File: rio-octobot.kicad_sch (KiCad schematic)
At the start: 48 parts, among them J1 Conn_01x06, J10 Conn_01x03, J2 Conn_01x06, J3 Conn_01x06, J4 Conn_01x06, J5 Conn_01x06, J6 Conn_01x06, J7 Conn_01x06, J8 Conn_01x06, J9 Conn_01x03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

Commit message: fixing labels / add some values
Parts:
- R1: value R -> 10k
- R1: value R -> 1k
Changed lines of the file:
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@@
     (stroke (width 0) (type default))
   )
-  (wire (pts (xy 146.05 60.96) (xy 173.99 60.96))
+  (wire (pts (xy 146.05 59.69) (xy 173.99 59.69))
     (stroke (width 0) (type default))
   )
@@
     (stroke (width 0) (type default))
   )
-  (wire (pts (xy 173.99 60.96) (xy 173.99 58.42))
+  (wire (pts (xy 173.99 59.69) (xy 173.99 58.42))
     (stroke (width 0) (type default))
   )
@@
     (stroke (width 0) (type default))
   )
+  (wire (pts (xy 146.05 53.34) (xy 146.05 59.69))
+    (stroke (width 0) (type default))
+  )
   (wire (pts (xy 210.82 45.72) (xy 210.82 54.61))
     (stroke (width 0) (type default))
@@
     (stroke (width 0) (type default))
   )
-  (wire (pts (xy 146.05 53.34) (xy 146.05 60.96))
-    (stroke (width 0) (type default))
-  )
   (wire (pts (xy 146.05 45.72) (xy 146.05 48.26))
     (stroke (width 0) (type default))
@@
     )
   )
-  (global_label "gnd" (shape input) (at 146.05 53.34 180) (fields_autoplaced)
+  (global_label "gnd" (shape input) (at 146.05 59.69 180) (fields_autoplaced)
     (effects (font (size 1.27 1.27)) (justify right))
-    (property "Intersheetrefs" "${INTERSHEET_REFS}" (at 139.6972 53.34 0)
+    (property "Intersheetrefs" "${INTERSHEET_REFS}" (at 139.6972 59.69 0)
       (effects (font (size 1.27 1.27)) (justify right) hide)
     )
@@
   )
   (symbol (lib_id "Device:R") (at 149.86 45.72 90) (unit 1)
-    (in_bom yes) (on_board yes) (dnp no) (fields_autoplaced)
-    (property "Reference" "R1" (at 149.86 39.37 90)
+    (in_bom yes) (on_board yes) (dnp no)
+    (property "Reference" "R1" (at 143.51 45.72 90)
       (effects (font (size 1.27 1.27)))
     )
-    (property "Value" "R" (at 149.86 41.91 90)
+    (property "Value" "10k" (at 154.94 46.99 90)
       (effects (font (size 1.27 1.27)))
     )
@@
   )
   (symbol (lib_id "Device:R") (at 149.86 38.1 90) (unit 1)
-    (in_bom yes) (on_board yes) (dnp no) (fields_autoplaced)
-    (property "Reference" "R1" (at 149.86 31.75 90)
+    (in_bom yes) (on_board yes) (dnp no)
+    (property "Reference" "R1" (at 143.51 38.1 90)
       (effects (font (size 1.27 1.27)))
     )
-    (property "Value" "R" (at 149.86 34.29 90)
+    (property "Value" "10k" (at 154.94 39.37 90)
       (effects (font (size 1.27 1.27)))
     )
@@
   )
   (symbol (lib_id "Device:R") (at 149.86 50.8 90) (unit 1)
-    (in_bom yes) (on_board yes) (dnp no) (fields_autoplaced)
-    (property "Reference" "R1" (at 149.86 44.45 90)
+    (in_bom yes) (on_board yes) (dnp no)
+    (property "Reference" "R1" (at 143.51 50.8 90)
       (effects (font (size 1.27 1.27)))
     )
-    (property "Value" "R" (at 149.86 46.99 90)
+    (property "Value" "10k" (at 154.94 52.07 90)
       (effects (font (size 1.27 1.27)))
     )
@@
   )
   (symbol (lib_id "Device:R") (at 149.86 53.34 90) (unit 1)
-    (in_bom yes) (on_board yes) (dnp no) (fields_autoplaced)
-    (property "Reference" "R1" (at 149.86 46.99 90)
+    (in_bom yes) (on_board yes) (dnp no)
+    (property "Reference" "R1" (at 143.51 53.34 90)
       (effects (font (size 1.27 1.27)))
     )
-    (property "Value" "R" (at 149.86 49.53 90)
+    (property "Value" "10k" (at 154.94 54.61 90)
       (effects (font (size 1.27 1.27)))
     )
@@
   )
   (symbol (lib_id "Device:R") (at 149.86 43.18 90) (unit 1)
-    (in_bom yes) (on_board yes) (dnp no) (fields_autoplaced)
-    (property "Reference" "R1" (at 149.86 36.83 90)
+    (in_bom yes) (on_board yes) (dnp no)
+    (property "Reference" "R1" (at 143.51 43.18 90)
       (effects (font (size 1.27 1.27)))
     )
-    (property "Value" "R" (at 149.86 39.37 90)
+    (property "Value" "10k" (at 154.94 44.45 90)
       (effects (font (size 1.27 1.27)))
     )
@@
   )
   (symbol (lib_id "Device:R") (at 149.86 40.64 90) (unit 1)
-    (in_bom yes) (on_board yes) (dnp no) (fields_autoplaced)
-    (property "Reference" "R1" (at 149.86 34.29 90)
+    (in_bom yes) (on_board yes) (dnp no)
+    (property "Reference" "R1" (at 143.51 40.64 90)
       (effects (font (size 1.27 1.27)))
     )
-    (property "Value" "R" (at 149.86 36.83 90)
+    (property "Value" "10k" (at 154.94 41.91 90)
       (effects (font (size 1.27 1.27)))
     )
@@
   )
   (symbol (lib_id "Device:R") (at 149.86 48.26 90) (unit 1)
-    (in_bom yes) (on_board yes) (dnp no) (fields_autoplaced)
-    (property "Reference" "R1" (at 149.86 41.91 90)
+    (in_bom yes) (on_board yes) (dnp no)
+    (property "Reference" "R1" (at 143.51 48.26 90)
       (effects (font (size 1.27 1.27)))
     )
-    (property "Value" "R" (at 149.86 44.45 90)
+    (property "Value" "10k" (at 154.94 49.53 90)
       (effects (font (size 1.27 1.27)))
     )
@@
       (effects (font (size 1.27 1.27)))
     )
-    (property "Value" "R" (at 196.85 107.95 90)
+    (property "Value" "1k" (at 196.85 107.95 90)
       (effects (font (size 1.27 1.27)))
     )
@@
       (effects (font (size 1.27 1.27)))
     )
-    (property "Value" "R" (at 201.93 138.43 90)
+    (property "Value" "10k" (at 201.93 138.43 90)
       (effects (font (size 1.27 1.27)))
     )
@@
   )
   (symbol (lib_id "Device:R") (at 187.96 147.32 90) (unit 1)
-    (in_bom yes) (on_board yes) (dnp no) (fields_autoplaced)
-    (property "Reference" "R1" (at 187.96 140.97 90)
+    (in_bom yes) (on_board yes) (dnp no)
+    (property "Reference" "R1" (at 187.96 144.78 90)
       (effects (font (size 1.27 1.27)))
     )
-    (property "Value" "R" (at 187.96 143.51 90)
+    (property "Value" "1k" (at 187.96 149.86 90)
       (effects (font (size 1.27 1.27)))
     )
@@
       (effects (font (size 1.27 1.27)) (justify right))
     )
-    (property "Value" "R" (at 193.04 116.84 0)
+    (property "Value" "10k" (at 193.04 116.84 0)
       (effects (font (size 1.27 1.27)) (justify right))
     )
@@
   )
   (symbol (lib_id "Device:R") (at 149.86 35.56 90) (unit 1)
-    (in_bom yes) (on_board yes) (dnp no) (fields_autoplaced)
-    (property "Reference" "R1" (at 149.86 29.21 90)
+    (in_bom yes) (on_board yes) (dnp no)
+    (property "Reference" "R1" (at 143.51 35.56 90)
       (effects (font (size 1.27 1.27)))
     )
-    (property "Value" "R" (at 149.86 31.75 90)
+    (property "Value" "10k" (at 154.94 36.83 90)
       (effects (font (size 1.27 1.27)))
     )

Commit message: removing level shifter from wled
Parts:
- removed Q2: BC817, Package_TO_SOT_SMD:SOT-23, symbol Transistor_BJT:BC817
- removed R1: 10k, Resistor_SMD:R_1206_3216Metric, symbol Device:R
- removed R1: 1k, Resistor_SMD:R_1206_3216Metric, symbol Device:R
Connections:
- net m7: now also D1.4 (DIN)
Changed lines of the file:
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@@
   (junction (at 146.05 50.8) (diameter 0) (color 0 0 0 0)
   )
-  (junction (at 215.9 135.89) (diameter 0) (color 0 0 0 0)
-  )
   (junction (at 62.23 102.87) (diameter 0) (color 0 0 0 0)
   )
-  (junction (at 198.12 142.24) (diameter 0) (color 0 0 0 0)
-  )
   (junction (at 215.9 152.4) (diameter 0) (color 0 0 0 0)
   )
@@
   (junction (at 213.36 82.55) (diameter 0) (color 0 0 0 0)
   )
-  (junction (at 205.74 135.89) (diameter 0) (color 0 0 0 0)
-  )
   (junction (at 213.36 36.83) (diameter 0) (color 0 0 0 0)
   )
@@
     (stroke (width 0) (type default))
   )
-  (wire (pts (xy 198.12 143.51) (xy 198.12 142.24))
-    (stroke (width 0) (type default))
-  )
   (wire (pts (xy 153.67 93.98) (xy 163.83 93.98))
     (stroke (width 0) (type default))
   )
-  (wire (pts (xy 184.15 147.32) (xy 182.88 147.32))
-    (stroke (width 0) (type default))
-  )
   (wire (pts (xy 146.05 99.06) (xy 146.05 106.68))
     (stroke (width 0) (type default))
@@
     (stroke (width 0) (type default))
   )
-  (wire (pts (xy 204.47 135.89) (xy 205.74 135.89))
-    (stroke (width 0) (type default))
-  )
   (wire (pts (xy 62.23 86.36) (xy 66.04 86.36))
     (stroke (width 0) (type default))
@@
     (stroke (width 0) (type default))
   )
-  (wire (pts (xy 191.77 147.32) (xy 190.5 147.32))
-    (stroke (width 0) (type default))
-  )
   (wire (pts (xy 184.15 48.26) (xy 194.31 48.26))
     (stroke (width 0) (type default))
@@
     (stroke (width 0) (type default))
   )
-  (wire (pts (xy 205.74 135.89) (xy 215.9 135.89))
-    (stroke (width 0) (type default))
-  )
   (wire (pts (xy 205.74 38.1) (xy 205.74 36.83))
     (stroke (width 0) (type default))
@@
   )
   (wire (pts (xy 153.67 99.06) (xy 163.83 99.06))
-    (stroke (width 0) (type default))
-  )
-  (wire (pts (xy 198.12 135.89) (xy 198.12 142.24))
     (stroke (width 0) (type default))
   )
@@
     )
   )
-  (global_label "m7" (shape input) (at 182.88 147.32 180) (fields_autoplaced)
-    (effects (font (size 1.27 1.27)) (justify right))
-    (property "Intersheetrefs" "${INTERSHEET_REFS}" (at 177.0714 147.32 0)
+  (global_label "m7" (shape input) (at 198.12 143.51 180) (fields_autoplaced)
+    (effects (font (size 1.27 1.27)) (justify right))
+    (property "Intersheetrefs" "${INTERSHEET_REFS}" (at 192.3114 143.51 0)
       (effects (font (size 1.27 1.27)) (justify right) hide)
     )
@@
         (path "/c4675d0b-5c1c-444a-a1ef-26bf66f46aa5"
           (reference "J1") (unit 1)
-        )
-      )
-    )
-  )
-  (symbol (lib_id "Transistor_BJT:BC817") (at 195.58 147.32 0) (unit 1)
-    (in_bom yes) (on_board yes) (dnp no) (fields_autoplaced)
-    (property "Reference" "Q2" (at 200.66 146.05 0)
-      (effects (font (size 1.27 1.27)) (justify left))
-    )
-    (property "Value" "BC817" (at 200.66 148.59 0)
-      (effects (font (size 1.27 1.27)) (justify left))
-    )
-    (property "Footprint" "Package_TO_SOT_SMD:SOT-23" (at 200.66 149.225 0)
-      (effects (font (size 1.27 1.27) italic) (justify left) hide)
-    )
-    (property "Datasheet" "https://www.onsemi.com/pub/Collateral/BC818-D.pdf" (at 195.58 147.32 0)
-      (effects (font (size 1.27 1.27)) (justify left) hide)
-    )
-    (pin "1")
-    (pin "2")
-    (pin "3")
-    (instances
-      (project "rio-octobot"
-        (path "/c4675d0b-5c1c-444a-a1ef-26bf66f46aa5"
-          (reference "Q2") (unit 1)
         )
       )
@@
     )
   )
-  (symbol (lib_id "Device:R") (at 201.93 135.89 90) (unit 1)
-    (in_bom yes) (on_board yes) (dnp no)
-    (property "Reference" "R1" (at 201.93 133.35 90)
-      (effects (font (size 1.27 1.27)))
-    )
-    (property "Value" "10k" (at 201.93 138.43 90)
-      (effects (font (size 1.27 1.27)))
-    )
-    (property "Footprint" "Resistor_SMD:R_1206_3216Metric" (at 201.93 137.668 90)
-      (effects (font (size 1.27 1.27)) hide)
-    )
-    (property "Datasheet" "~" (at 201.93 135.89 0)
-      (effects (font (size 1.27 1.27)) hide)
-    )
-    (pin "1")
-    (pin "2")
-    (instances
-      (project "rio-octobot"
-        (path "/c4675d0b-5c1c-444a-a1ef-26bf66f46aa5/cda04744-3ce8-4a6b-a82d-a1325fcc2daa"
-          (reference "R1") (unit 1)
-        )
-        (path "/c4675d0b-5c1c-444a-a1ef-26bf66f46aa5/c87ea30f-b16d-4690-be9f-7e9196f340db"
-          (reference "R2") (unit 1)
-        )
-        (path "/c4675d0b-5c1c-444a-a1ef-26bf66f46aa5/0caef072-d6e6-4191-8609-a2a060f30d09"
-          (reference "R3") (unit 1)
-        )
-        (path "/c4675d0b-5c1c-444a-a1ef-26bf66f46aa5/9b7eb7c2-dba6-4078-aea0-2fd449da534f"
-          (reference "R4") (unit 1)
-        )
-        (path "/c4675d0b-5c1c-444a-a1ef-26bf66f46aa5/c4b53cc4-45b0-40c6-a2e4-f85052d4ed8a"
-          (reference "R5") (unit 1)
-        )
-        (path "/c4675d0b-5c1c-444a-a1ef-26bf66f46aa5/6dac5bea-3ac5-4905-a711-17de9963fb48"
-          (reference "R6") (unit 1)
-        )
-        (path "/c4675d0b-5c1c-444a-a1ef-26bf66f46aa5/0e9d2bbf-2b0b-4860-a06b-304bc4546dd9"
-          (reference "R7") (unit 1)
-        )
-        (path "/c4675d0b-5c1c-444a-a1ef-26bf66f46aa5/77b70234-a638-4cba-af0b-c8e26a05632f"
-          (reference "R8") (unit 1)
-        )
-        (path "/c4675d0b-5c1c-444a-a1ef-26bf66f46aa5/341fad45-713c-4626-966f-e3afd8f08c91"
-          (reference "R16") (unit 1)
-        )
-        (path "/c4675d0b-5c1c-444a-a1ef-26bf66f46aa5"
-          (reference "R52") (unit 1)
-        )
-      )
-    )
-  )
   (symbol (lib_id "Connector_Generic:Conn_02x18_Odd_Even") (at 35.56 49.53 0) (unit 1)
     (in_bom yes) (on_board yes) (dnp no) (fields_autoplaced)
@@
         )
       )
-    )
-  )
-  (symbol (lib_id "Device:R") (at 187.96 147.32 90) (unit 1)
-    (in_bom yes) (on_board yes) (dnp no)
-    (property "Reference" "R1" (at 187.96 144.78 90)
-      (effects (font (size 1.27 1.27)))
-    )
-    (property "Value" "1k" (at 187.96 149.86 90)
-      (effects (font (size 1.27 1.27)))
-    )
-    (property "Footprint" "Resistor_SMD:R_1206_3216Metric" (at 187.96 149.098 90)
-      (effects (font (size 1.27 1.27)) hide)
-    )
-    (property "Datasheet" "~" (at 187.96 147.32 0)
-      (effects (font (size 1.27 1.27)) hide)
-    )
-    (pin "1")
-    (pin "2")
-    (instances
-      (project "rio-octobot"
-        (path "/c4675d0b-5c1c-444a-a1ef-26bf66f46aa5/cda04744-3ce8-4a6b-a82d-a1325fcc2daa"
-          (reference "R1") (unit 1)
-        )
-        (path "/c4675d0b-5c1c-444a-a1ef-26bf66f46aa5/c87ea30f-b16d-4690-be9f-7e9196f340db"
-          (reference "R2") (unit 1)
-        )
-        (path "/c4675d0b-5c1c-444a-a1ef-26bf66f46aa5/0caef072-d6e6-4191-8609-a2a060f30d09"
-          (reference "R3") (unit 1)
-        )
-        (path "/c4675d0b-5c1c-444a-a1ef-26bf66f46aa5/9b7eb7c2-dba6-4078-aea0-2fd449da534f"
-          (reference "R4") (unit 1)
-        )
-        (path "/c4675d0b-5c1c-444a-a1ef-26bf66f46aa5/c4b53cc4-45b0-40c6-a2e4-f85052d4ed8a"
-          (reference "R5") (unit 1)
-        )
-        (path "/c4675d0b-5c1c-444a-a1ef-26bf66f46aa5/6dac5bea-3ac5-4905-a711-17de9963fb48"
-          (reference "R6") (unit 1)
-        )
-        (path "/c4675d0b-5c1c-444a-a1ef-26bf66f46aa5/0e9d2bbf-2b0b-4860-a06b-304bc4546dd9"
-          (reference "R7") (unit 1)
-        )
-        (path "/c4675d0b-5c1c-444a-a1ef-26bf66f46aa5/77b70234-a638-4cba-af0b-c8e26a05632f"
-          (reference "R8") (unit 1)
-        )
-        (path "/c4675d0b-5c1c-444a-a1ef-26bf66f46aa5/341fad45-713c-4626-966f-e3afd8f08c91"
-          (reference "R16") (unit 1)
-        )
-        (path "/c4675d0b-5c1c-444a-a1ef-26bf66f46aa5"
-          (reference "R49") (unit 1)
-        )
-      )

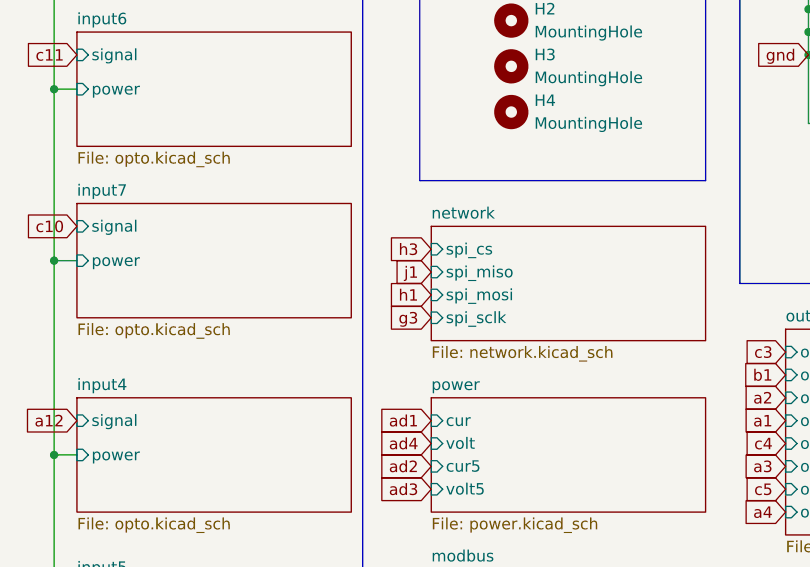
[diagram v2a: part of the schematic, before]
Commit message: chaning network interface to W5500
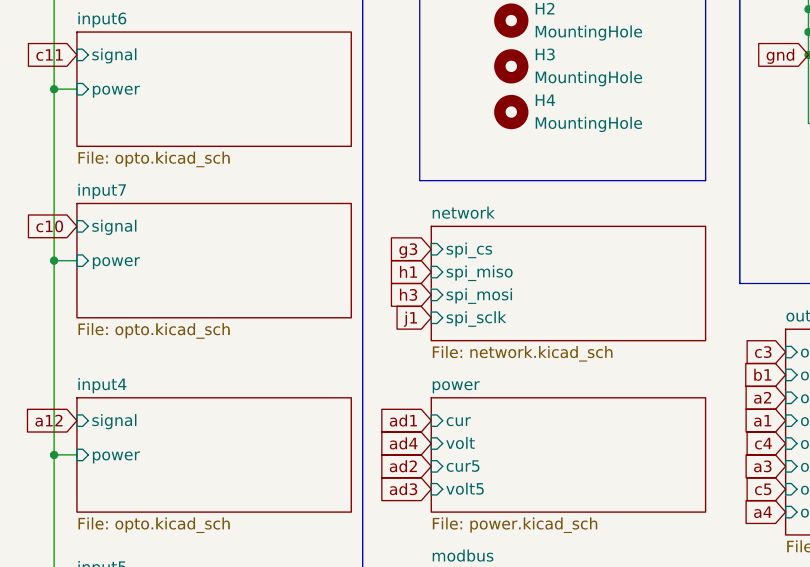
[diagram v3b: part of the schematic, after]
